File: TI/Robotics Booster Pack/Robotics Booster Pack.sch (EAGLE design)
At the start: 119 parts, among them U10 74LVTH125.RGY, U11 SCHA4B0400, U12 BLUETOOTH-RN41", U13 XBEE-1XBEE-1_LOCK, U5 TPS5331[8/9].DQP, U6 TPS62082.DSG, U7 PCA9557.RGV, U8 MPU-6050

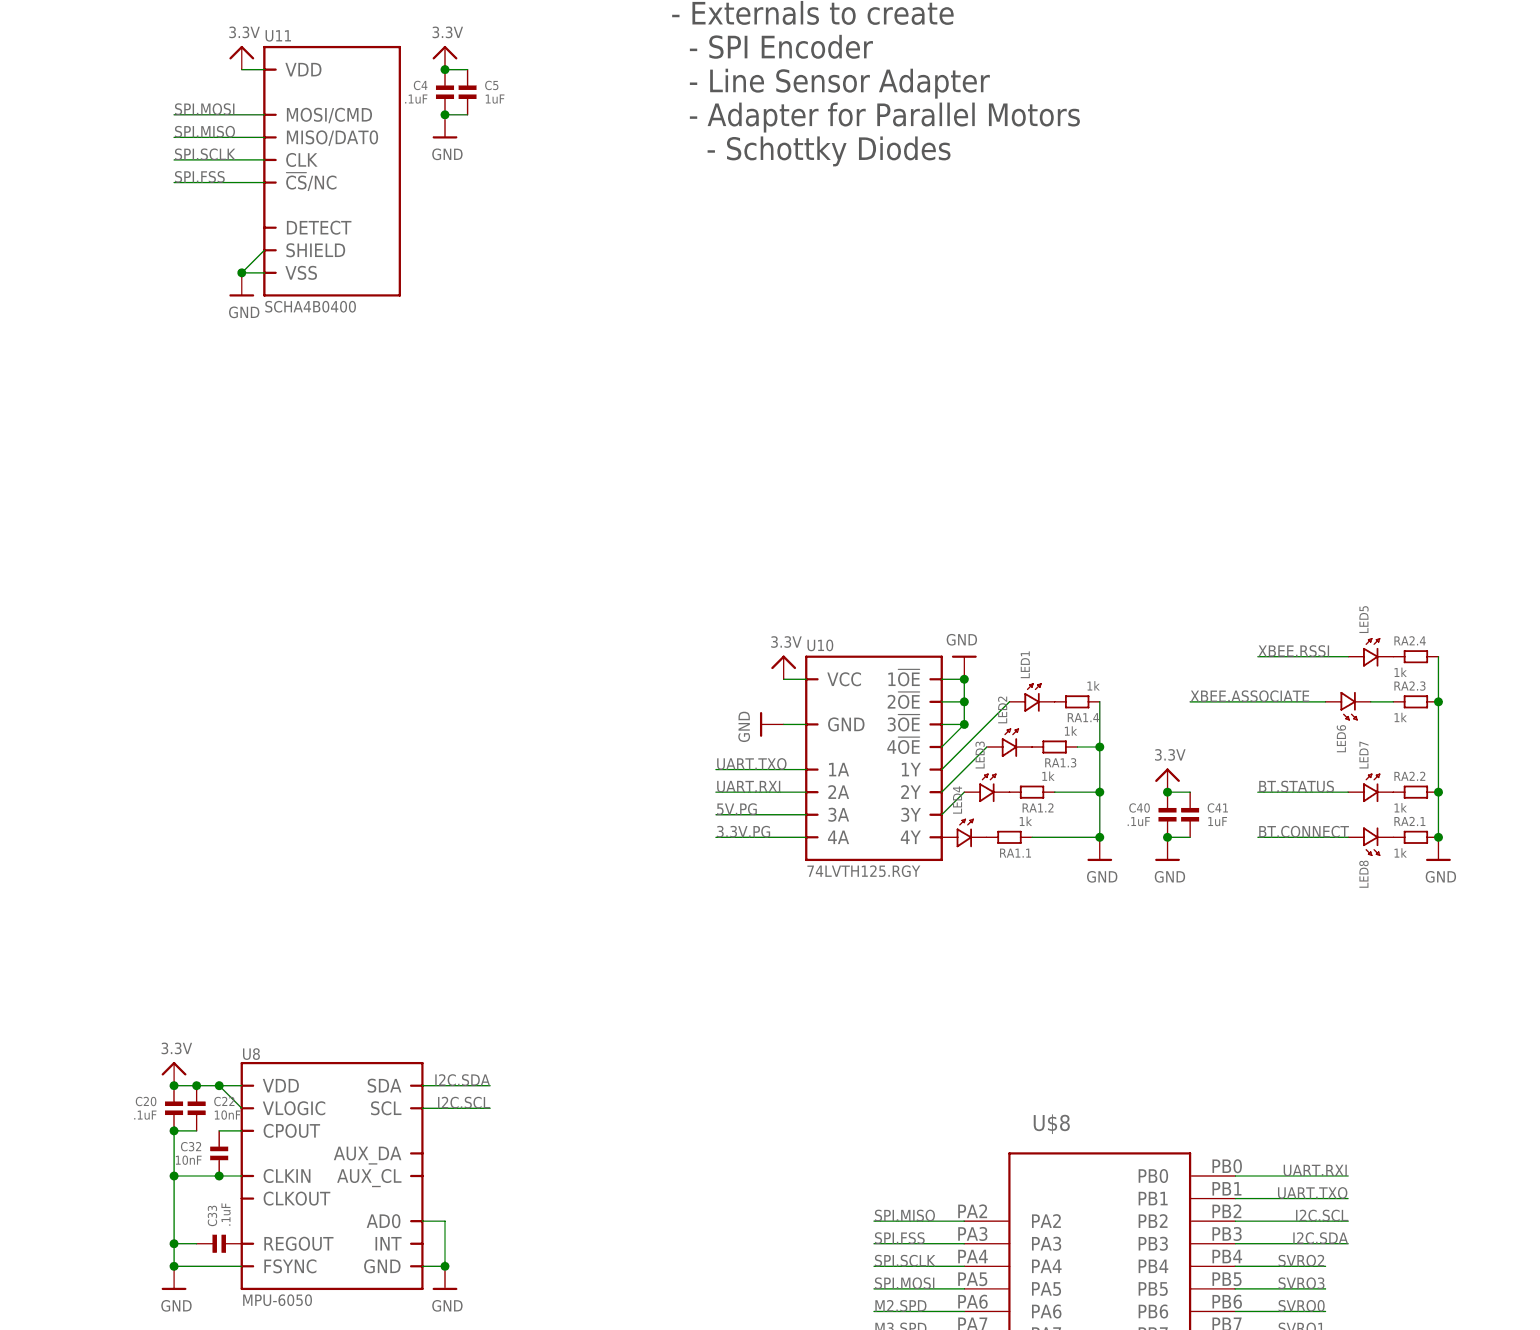
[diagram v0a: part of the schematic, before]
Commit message: Renamed files. Corrected uSD Card package. All other ICs check out.
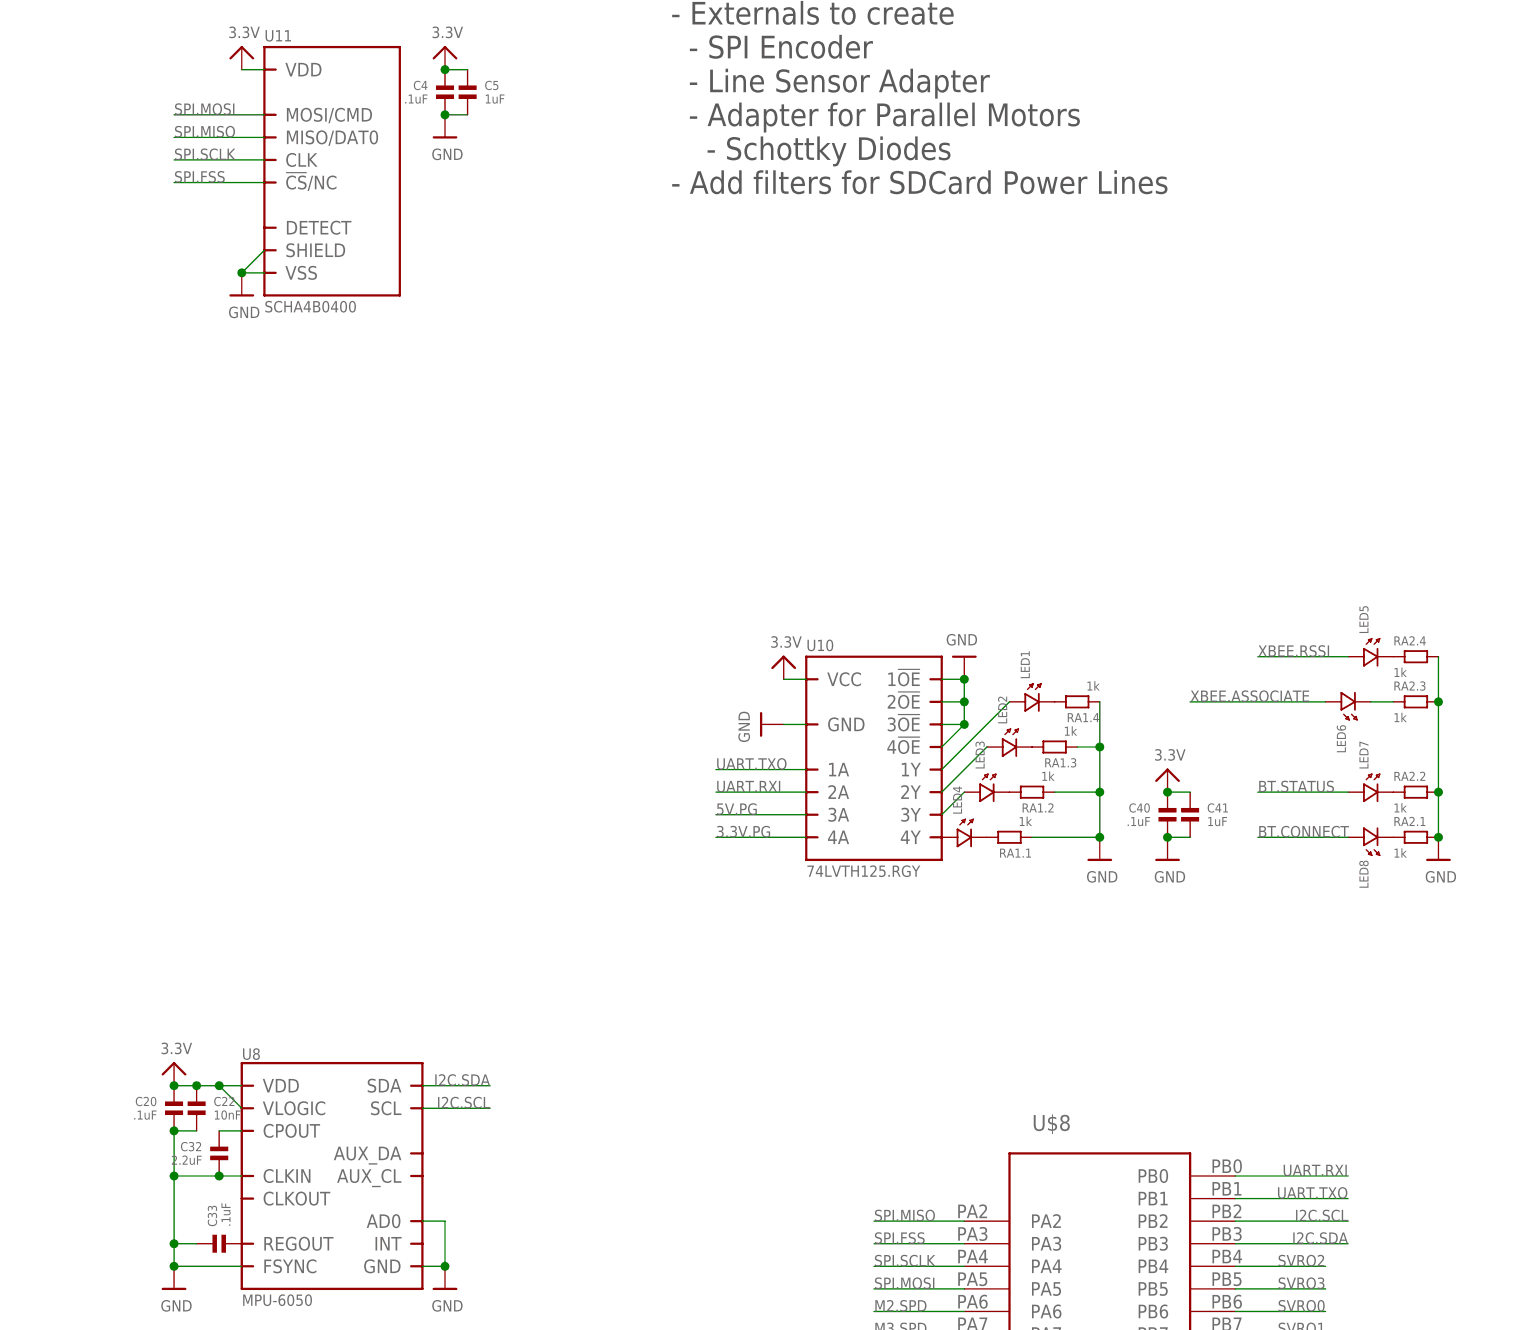
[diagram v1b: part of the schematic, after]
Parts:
- C32: value 10nF -> 2.2uF
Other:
- note added: "NOTES: - Remove R9 & R10 to decouple B[6/7] from D[0/1] - Externals to create - SPI Encoder - Line Sensor Adapter - Adapter for Parallel Motors - Schottky Diodes - Add filters for SDCard Power Lines"
- note removed: "NOTES: - Remove R9 & R10 to decouple B[6/7] from D[0/1] - Externals to create - SPI Encoder - Line Sensor Adapter - Adapter for Parallel Motors - Schottky Diodes"
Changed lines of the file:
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@@
 <part name="C20" library="standardparts" deviceset="CAPACITOR" device=".0603" value=".1uF"/>
 <part name="C22" library="standardparts" deviceset="CAPACITOR" device=".0603" value="10nF"/>
-<part name="C32" library="standardparts" deviceset="CAPACITOR" device=".0603" value="10nF"/>
+<part name="C32" library="standardparts" deviceset="CAPACITOR" device=".0603" value="2.2uF"/>
 <part name="C33" library="standardparts" deviceset="CAPACITOR" device=".0603" value=".1uF"/>
 <part name="U$114" library="microbuilder" deviceset="GND" device=""/>
@@
   - Line Sensor Adapter
   - Adapter for Parallel Motors
-    - Schottky Diodes</text>
+    - Schottky Diodes
+- Add filters for SDCard Power Lines</text>
 </plain>
 <instances>

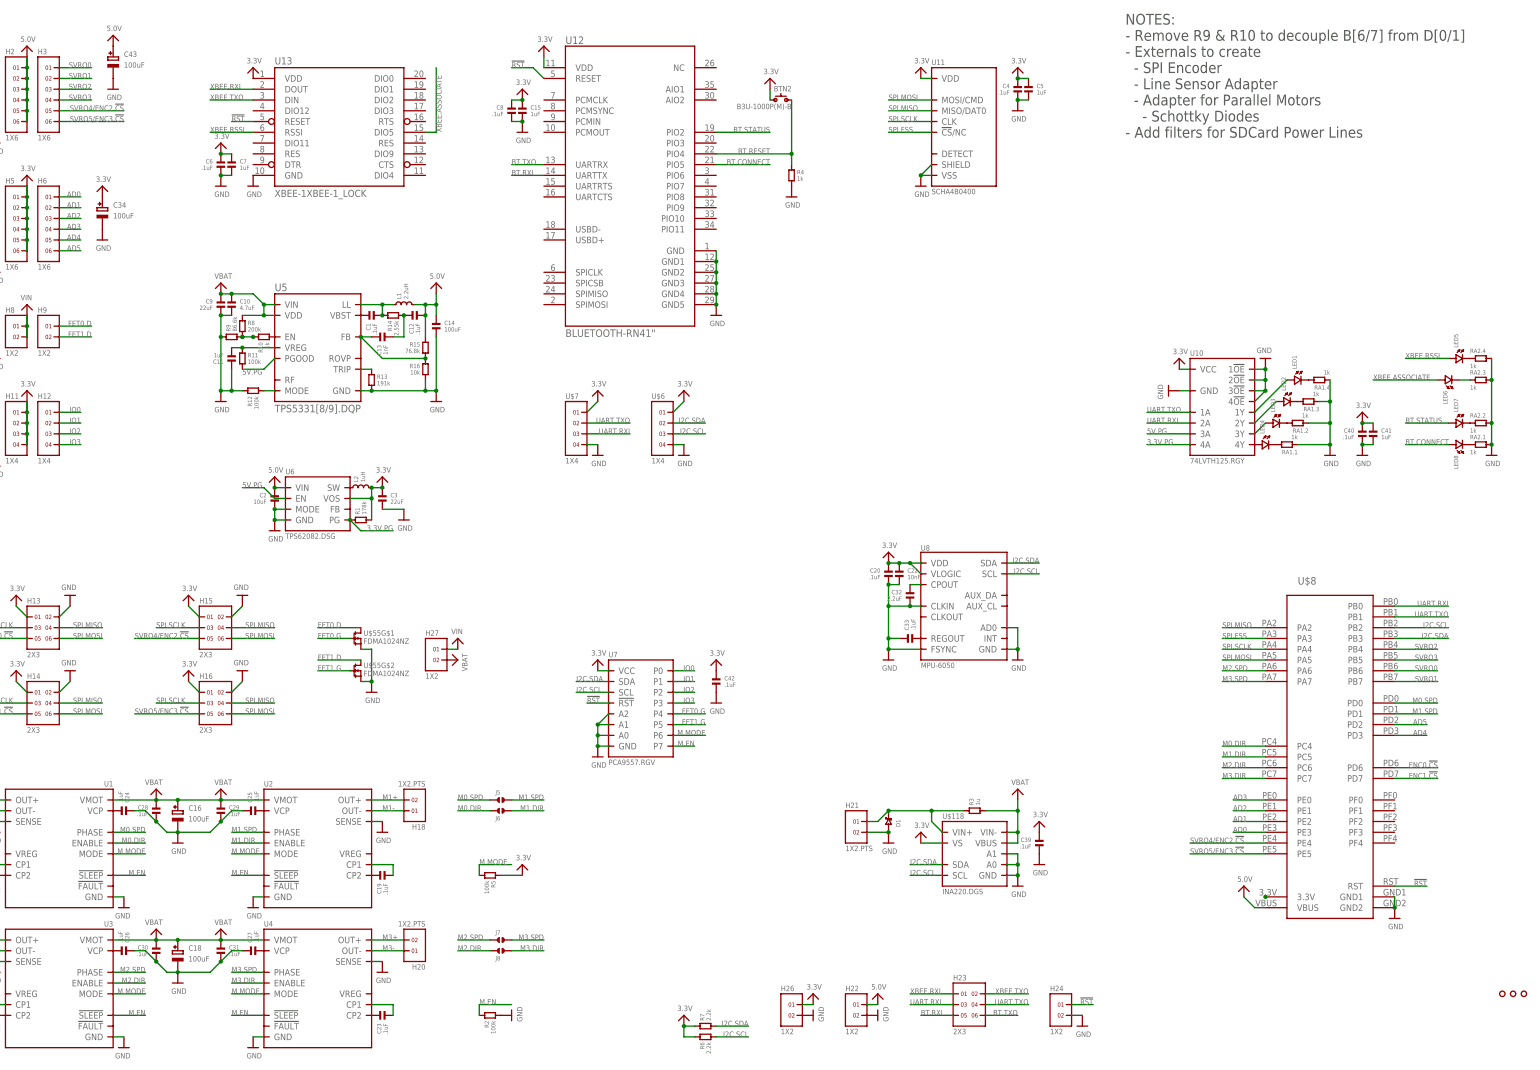
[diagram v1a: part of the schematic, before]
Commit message: Creating base board for Pololu Black Motor Mount
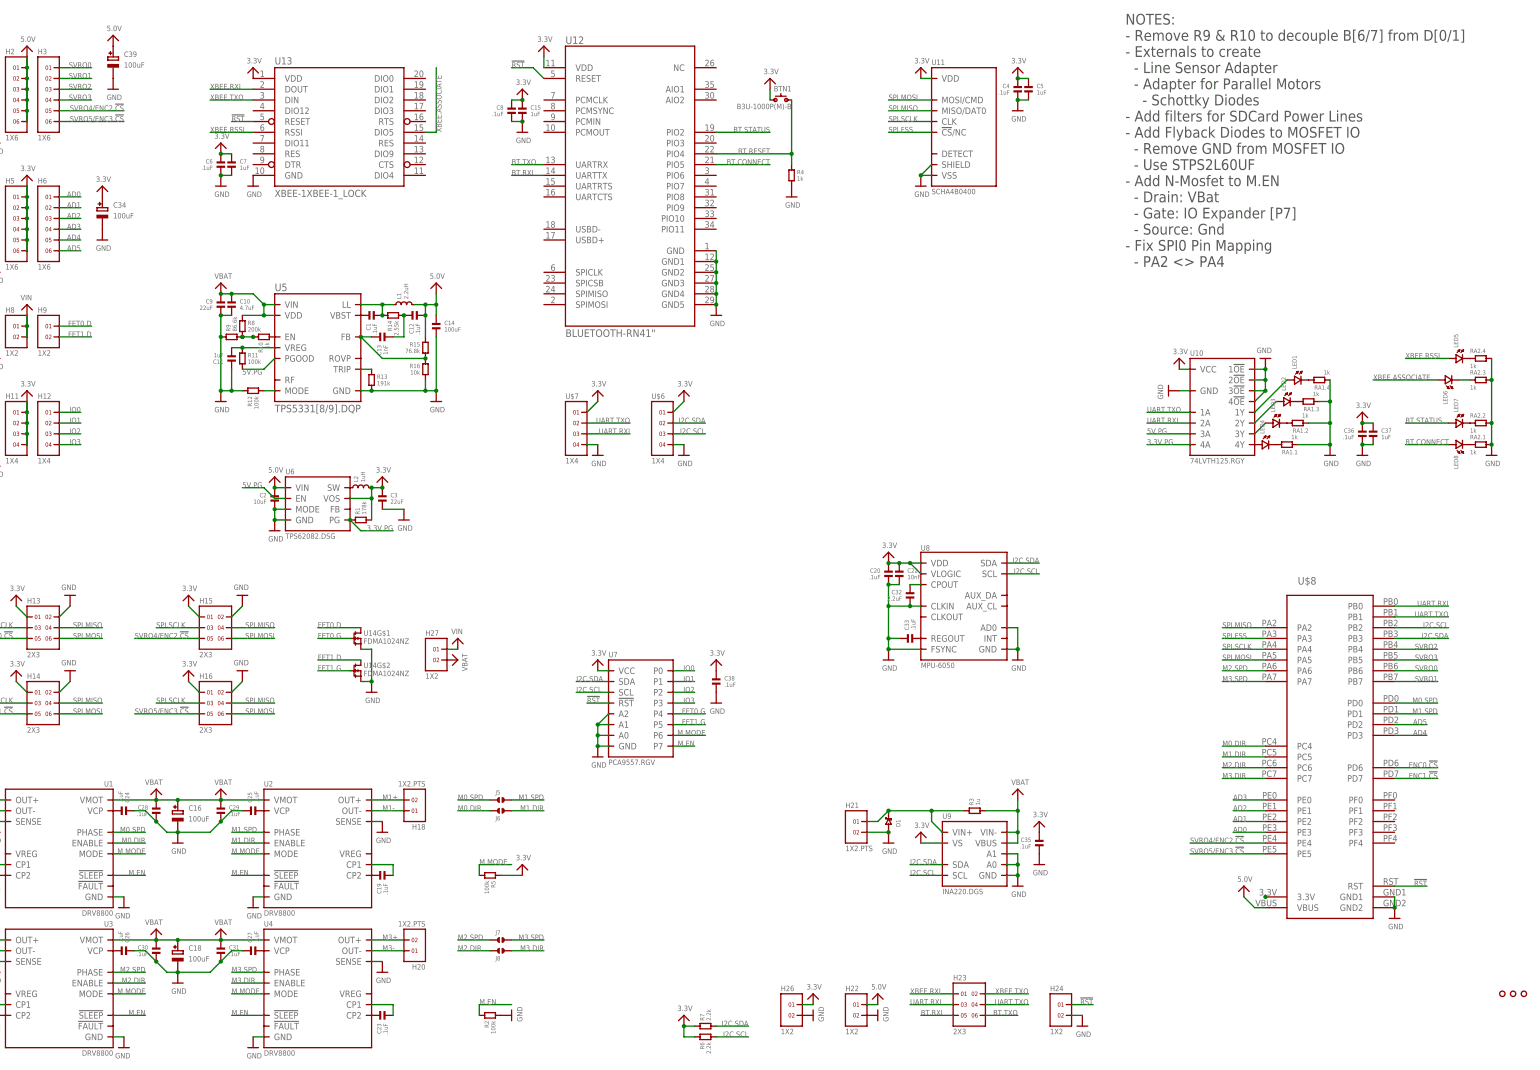
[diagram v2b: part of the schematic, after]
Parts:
- removed C43: 100uF, microbuilder:CAP_ELECTROLYTICPANASONIC_C
- added C35: .1uF, standardparts:CAPACITOR.0603
- C39: value .1uF -> 100uF; device standardparts:CAPACITOR.0603 -> microbuilder:CAP_ELECTROLYTICPANASONIC_C
- U1, U2, U3, U4: value (none) -> DRV8800
- renumbered BTN2 to BTN1, C40 to C36, C41 to C37, C42 to C38, U$118 to U9, U$55 to U14
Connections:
- net 3.3V: now also C35.1; no longer C39.1
- net 5.0V: now also C39.+; no longer C43.+
- net GND: now also C35.2, C39.-; no longer C39.2, C43.-
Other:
- note added: "NOTES: - Remove R9 & R10 to decouple B[6/7] from D[0/1] - Externals to create - Line Sensor Adapter - Adapter for Parallel Motors - Schottky Diodes - Add filters for SDCard Power Lines - Add Flyback Diodes to MOSFET IO - Remove GND from MOSFET IO - Use STPS2L60UF - Add N-Mosfet to M.EN - Drain: VBat - Gate: IO Expander [P7] - Source: Gnd - Fix SPI0 Pin Mapping - PA2 <> PA4"
- note removed: "NOTES: - Remove R9 & R10 to decouple B[6/7] from D[0/1] - Externals to create - SPI Encoder - Line Sensor Adapter - Adapter for Parallel Motors - Schottky Diodes - Add filters for SDCard Power Lines"
